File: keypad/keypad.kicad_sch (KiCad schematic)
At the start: 67 parts, among them J1 NO FIT, J2 NO FIT, P1 GT-USB-7010ASV, Q1 BC807-40LT1G, SW1 TS04-66-70-BK-100-SMT, SW2 TS04-66-70-BK-100-SMT, SW4 NO FIT, SW5 NO FIT, U1 RP2040, U2 LM4040DBZ-2.0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

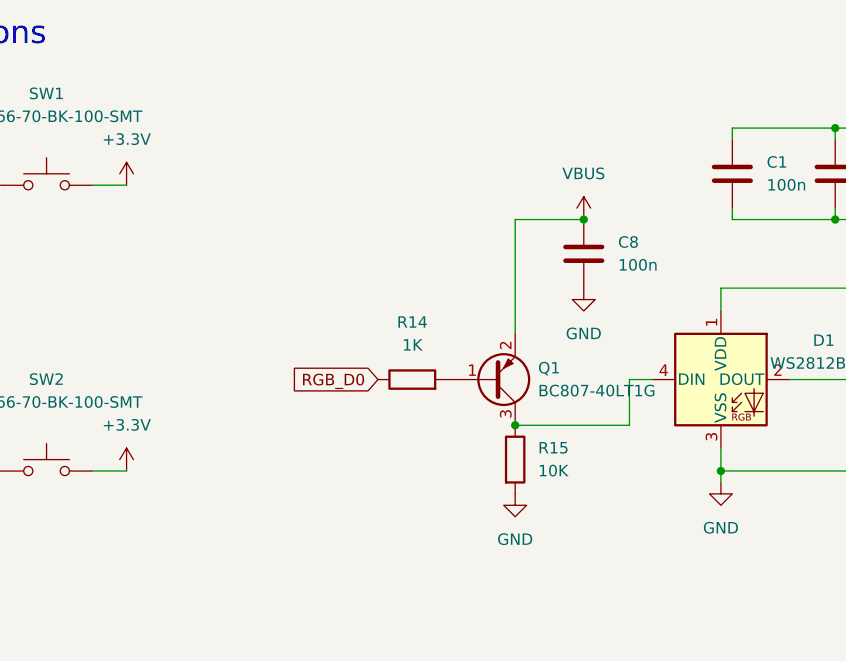
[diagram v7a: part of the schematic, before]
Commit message: ditch rev3a for rev3b
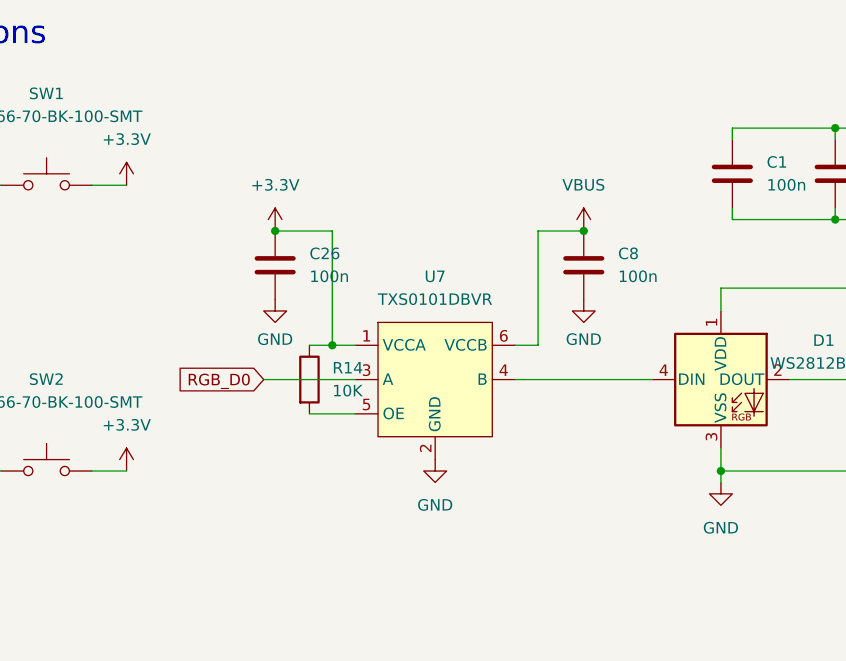
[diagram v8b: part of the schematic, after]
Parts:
- removed Q1: BC807-40LT1G, Package_TO_SOT_SMD:SOT-23, symbol Transistor_BJT:BC807
- removed R15: 10K, Resistor_SMD:R_0805_2012Metric, symbol Device:R
- added C26: 100n, Capacitor_SMD:C_0805_2012Metric, symbol Device:C
- added U7: TXS0101DBVR, Package_TO_SOT_SMD:SOT-23-6, symbol Custom_Parts:TXS0101DBVR
- R14: value 1K -> 10K
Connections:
- net +3.3V: now also R14.1, C26.1, U7.1 (VCCA)
- net GND: now also C26.2, U7.2 (GND)
- net RGB_D0: now also U7.3 (A); no longer R14.1
- net VBUS: now also U7.6 (VCCB)
- net at D1.4 (DIN): now also U7.4 (B)
- net at R14.2: now also U7.5 (OE)
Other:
- moved on the sheet: C8
